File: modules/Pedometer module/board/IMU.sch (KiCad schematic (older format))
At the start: 2 parts, among them U3 LSM6DS3

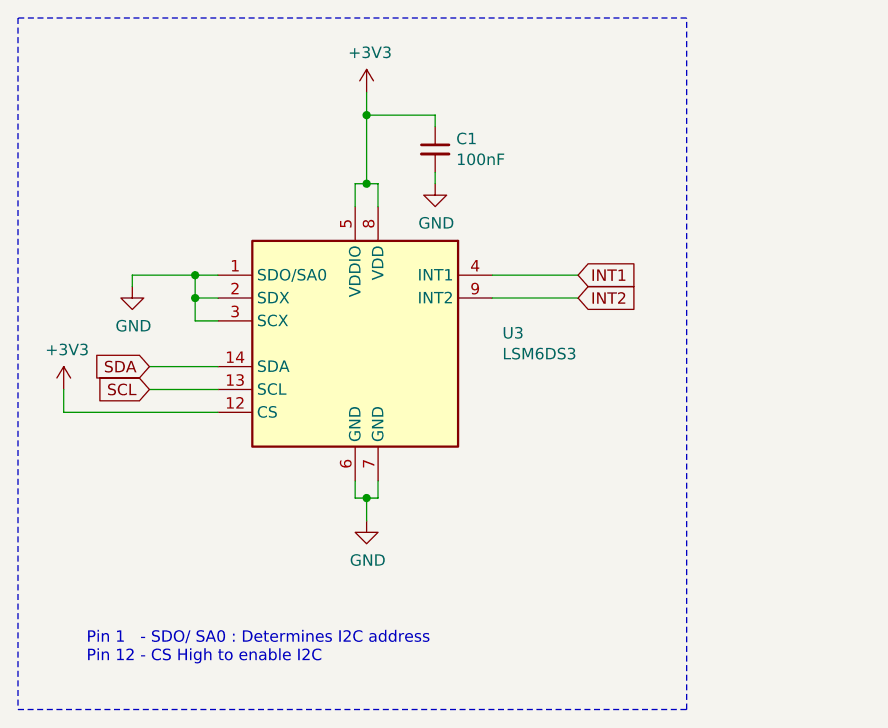
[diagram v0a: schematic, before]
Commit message: Fix I2C pullup resistor
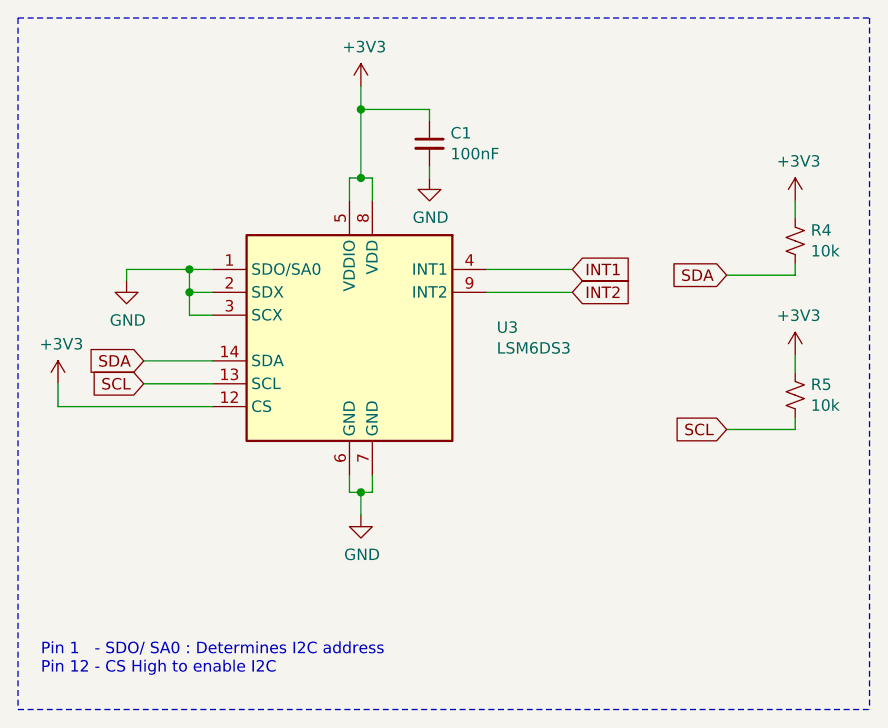
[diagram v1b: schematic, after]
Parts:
- added R4, R5: 10k, Resistor_SMD:R_0805_2012Metric_Pad1.20x1.40mm_HandSolder, symbol Device:R_Small_US
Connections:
- net +3V3: now also R4.1, R5.1
- net SCL: now also R5.2
- net SDA: now also R4.2
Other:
- moved on the sheet: C1, U3
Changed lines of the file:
@@
 Comment4 ""
 $EndDescr
+Wire Wire Line
+	5500 2750 5500 2850
+$Comp
+L power:GND #PWR09
+U 1 1 63A2C7F2
+P 5450 4225
+F 0 "#PWR09" H 5450 3975 50  0001 C CNN
+F 1 "GND" H 5455 4052 50  0000 C CNN
+F 2 "" H 5450 4225 50  0001 C CNN
+F 3 "" H 5450 4225 50  0001 C CNN
+	1    5450 4225
+	1    0    0    -1
+$EndComp
+Wire Wire Line
+	5400 4125 5400 4050
+Wire Wire Line
+	5400 4125 5450 4125
+Wire Wire Line
+	5450 4125 5450 4225
+Wire Wire Line
+	5500 4050 5500 4125
+Wire Wire Line
+	5500 4125 5450 4125
+Connection ~ 5450 4125
+Wire Wire Line
+	6000 3150 6375 3150
+Wire Wire Line
+	6000 3250 6375 3250
+Wire Wire Line
+	4800 3550 4500 3550
+Wire Wire Line
+	4800 3650 4500 3650
+Text GLabel 6375 3150 2    50   Input ~ 0
+INT1
+Text GLabel 6375 3250 2    50   Input ~ 0
+INT2
+Text GLabel 4500 3650 0    50   Input ~ 0
+SCL
+Text GLabel 4500 3550 0    50   Input ~ 0
+SDA
+$Comp
+L power:GND #PWR05
+U 1 1 63A35DA4
+P 4425 3200
+F 0 "#PWR05" H 4425 2950 50  0001 C CNN
+F 1 "GND" H 4430 3027 50  0000 C CNN
+F 2 "" H 4425 3200 50  0001 C CNN
+F 3 "" H 4425 3200 50  0001 C CNN
+	1    4425 3200
+	1    0    0    -1
+$EndComp
+Wire Wire Line
+	4425 3200 4425 3150
+Wire Wire Line
+	4800 3250 4700 3250
+Wire Wire Line
+	4700 3250 4700 3150
+Wire Wire Line
+	4700 3150 4800 3150
+Wire Wire Line
+	4800 3350 4700 3350
+Wire Wire Line
+	4700 3350 4700 3250
+Connection ~ 4700 3250
+Wire Wire Line
+	4425 3150 4700 3150
+Connection ~ 4700 3150
+Wire Wire Line
+	5400 2750 5400 2850
+$Comp
+L power:+3V3 #PWR07
+U 1 1 63A2BC7C
+P 5450 2350
+F 0 "#PWR07" H 5450 2200 50  0001 C CNN
+F 1 "+3V3" H 5465 2523 50  0000 C CNN
+F 2 "" H 5450 2350 50  0001 C CNN
+F 3 "" H 5450 2350 50  0001 C CNN
+	1    5450 2350
+	1    0    0    -1
+$EndComp
+$Comp
+L Device:C_Small C1
+U 1 1 63A39BBA
+P 5750 2600
+F 0 "C1" H 5842 2646 50  0000 L CNN
+F 1 "100nF" H 5842 2555 50  0000 L CNN
+F 2 "Capacitor_SMD:C_0805_2012Metric_Pad1.18x1.45mm_HandSolder" H 5750 2600 50  0001 C CNN
+F 3 "~" H 5750 2600 50  0001 C CNN
+	1    5750 2600
+	1    0    0    -1
+$EndComp
+Wire Wire Line
+	5400 2750 5450 2750
+$Comp
+L power:GND #PWR010
+U 1 1 63A3AF6F
+P 5750 2750
+F 0 "#PWR010" H 5750 2500 50  0001 C CNN
+F 1 "GND" H 5755 2577 50  0000 C CNN
+F 2 "" H 5750 2750 50  0001 C CNN
+F 3 "" H 5750 2750 50  0001 C CNN
+	1    5750 2750
+	1    0    0    -1
+$EndComp
+Wire Wire Line
+	5750 2750 5750 2700
+Connection ~ 5450 2750
+Wire Wire Line
+	5450 2750 5500 2750
+Wire Wire Line
+	5450 2350 5450 2450
+Wire Wire Line
+	5750 2500 5750 2450
+Wire Wire Line
+	5750 2450 5450 2450
+Connection ~ 5450 2450
+Wire Wire Line
+	5450 2450 5450 2750
+$Comp
+L power:+3V3 #PWR0109
+U 1 1 63A4A814
+P 4125 3650
+F 0 "#PWR0109" H 4125 3500 50  0001 C CNN
+F 1 "+3V3" H 4140 3823 50  0000 C CNN
+F 2 "" H 4125 3650 50  0001 C CNN
+F 3 "" H 4125 3650 50  0001 C CNN
+	1    4125 3650
+	1    0    0    -1
+$EndComp
+Wire Wire Line
+	4125 3650 4125 3750
+Wire Wire Line
+	4125 3750 4800 3750
+Text Notes 4050 4925 0    50   ~ 0
+Pin 1   - SDO/ SA0 : Determines I2C address\nPin 12 - CS High to enable I2C
+Wire Notes Line
+	3950 2050 3950 5075
+Wire Wire Line
+	7350 3800 7350 3850
+Wire Wire Line
+	7350 3525 7350 3600
+$Comp
+L power:+3V3 #PWR0110
+U 1 1 63B0AA74
+P 7350 3525
+F 0 "#PWR0110" H 7350 3375 50  0001 C CNN
+F 1 "+3V3" H 7365 3698 50  0000 C CNN
+F 2 "" H 7350 3525 50  0001 C CNN
+F 3 "" H 7350 3525 50  0001 C CNN
+	1    7350 3525
+	1    0    0    -1
+$EndComp
+Wire Wire Line
+	7350 3850 7050 3850
+Wire Wire Line
+	7350 3125 7350 3175
+Wire Wire Line
+	7350 2850 7350 2925
+$Comp
+L power:+3V3 #PWR0111
+U 1 1 63B08952
+P 7350 2850
+F 0 "#PWR0111" H 7350 2700 50  0001 C CNN
+F 1 "+3V3" H 7365 3023 50  0000 C CNN
+F 2 "" H 7350 2850 50  0001 C CNN
+F 3 "" H 7350 2850 50  0001 C CNN
+	1    7350 2850
+	1    0    0    -1
+$EndComp
+$Comp
+L Device:R_Small_US R4
+U 1 1 63B080DE
+P 7350 3025
+F 0 "R4" H 7418 3071 50  0000 L CNN
+F 1 "10k" H 7418 2980 50  0000 L CNN
+F 2 "Resistor_SMD:R_0805_2012Metric_Pad1.20x1.40mm_HandSolder" H 7350 3025 50  0001 C CNN
+F 3 "~" H 7350 3025 50  0001 C CNN
+	1    7350 3025
+	1    0    0    -1
+$EndComp
+Text GLabel 7050 3175 0    50   Input ~ 0
+SDA
+Text GLabel 7050 3850 0    50   Input ~ 0
+SCL
+Wire Wire Line
+	7350 3175 7050 3175
 $Comp
 L Sensor_Motion:LSM6DS3 U3
 U 1 1 63A2B005
-P 5425 3475
-F 0 "U3" H 6069 3521 50  0000 L CNN
-F 1 "LSM6DS3" H 6069 3430 50  0000 L CNN
-F 2 "Package_LGA:LGA-14_3x2.5mm_P0.5mm_LayoutBorder3x4y" H 5025 2775 50  0001 L CNN
-F 3 "www.st.com/resource/en/datasheet/lsm6ds3.pdf" H 5525 2825 50  0001 C CNN
-	1    5425 3475
-	1    0    0    -1
-$EndComp
-Wire Wire Line
-	5525 2775 5525 2875
-$Comp
-L power:GND #PWR09
-U 1 1 63A2C7F2
-P 5475 4250
-F 0 "#PWR09" H 5475 4000 50  0001 C CNN
-F 1 "GND" H 5480 4077 50  0000 C CNN
-F 2 "" H 5475 4250 50  0001 C CNN
-F 3 "" H 5475 4250 50  0001 C CNN
-	1    5475 4250
-	1    0    0    -1
-$EndComp
-Wire Wire Line
-	5425 4150 5425 4075
-Wire Wire Line
-	5425 4150 5475 4150
-Wire Wire Line
-	5475 4150 5475 4250
-Wire Wire Line
-	5525 4075 5525 4150
-Wire Wire Line
-	5525 4150 5475 4150
-Connection ~ 5475 4150
-Wire Wire Line
-	6025 3175 6400 3175
-Wire Wire Line
-	6025 3275 6400 3275
-Wire Wire Line
-	4825 3575 4525 3575
-Wire Wire Line
-	4825 3675 4525 3675
-Text GLabel 6400 3175 2    50   Input ~ 0
-INT1
-Text GLabel 6400 3275 2    50   Input ~ 0
-INT2
-Text GLabel 4525 3675 0    50   Input ~ 0
-SCL
-Text GLabel 4525 3575 0    50   Input ~ 0
-SDA
-$Comp
-L power:GND #PWR05
-U 1 1 63A35DA4
-P 4450 3225
-F 0 "#PWR05" H 4450 2975 50  0001 C CNN
-F 1 "GND" H 4455 3052 50  0000 C CNN
-F 2 "" H 4450 3225 50  0001 C CNN
-F 3 "" H 4450 3225 50  0001 C CNN
-	1    4450 3225
-	1    0    0    -1
-$EndComp
-Wire Wire Line
-	4450 3225 4450 3175
-Wire Wire Line
-	4825 3275 4725 3275
-Wire Wire Line
-	4725 3275 4725 3175
-Wire Wire Line
-	4725 3175 4825 3175
-Wire Wire Line
-	4825 3375 4725 3375
-Wire Wire Line
-	4725 3375 4725 3275
-Connection ~ 4725 3275
-Wire Wire Line
-	4450 3175 4725 3175
-Connection ~ 4725 3175
-Wire Wire Line
-	5425 2775 5425 2875
-$Comp
-L power:+3V3 #PWR07
-U 1 1 63A2BC7C
-P 5475 2375
-F 0 "#PWR07" H 5475 2225 50  0001 C CNN
-F 1 "+3V3" H 5490 2548 50  0000 C CNN
-F 2 "" H 5475 2375 50  0001 C CNN
-F 3 "" H 5475 2375 50  0001 C CNN
-	1    5475 2375
-	1    0    0    -1
-$EndComp
-$Comp
-L Device:C_Small C1
-U 1 1 63A39BBA
-P 5775 2625
-F 0 "C1" H 5867 2671 50  0000 L CNN
-F 1 "100nF" H 5867 2580 50  0000 L CNN
-F 2 "Capacitor_SMD:C_0805_2012Metric_Pad1.18x1.45mm_HandSolder" H 5775 2625 50  0001 C CNN
-F 3 "~" H 5775 2625 50  0001 C CNN
-	1    5775 2625
-	1    0    0    -1
-$EndComp
-Wire Wire Line
-	5425 2775 5475 2775
-$Comp
-L power:GND #PWR010
-U 1 1 63A3AF6F
-P 5775 2775
-F 0 "#PWR010" H 5775 2525 50  0001 C CNN
-F 1 "GND" H 5780 2602 50  0000 C CNN
-F 2 "" H 5775 2775 50  0001 C CNN
-F 3 "" H 5775 2775 50  0001 C CNN
-	1    5775 2775
-	1    0    0    -1
-$EndComp
-Wire Wire Line
-	5775 2775 5775 2725
-Connection ~ 5475 2775
-Wire Wire Line
-	5475 2775 5525 2775
-Wire Wire Line
-	5475 2375 5475 2475
-Wire Wire Line
-	5775 2525 5775 2475
-Wire Wire Line
-	5775 2475 5475 2475
-Connection ~ 5475 2475
-Wire Wire Line
-	5475 2475 5475 2775
-$Comp
-L power:+3V3 #PWR0109
-U 1 1 63A4A814
-P 4150 3675
-F 0 "#PWR0109" H 4150 3525 50  0001 C CNN
-F 1 "+3V3" H 4165 3848 50  0000 C CNN
-F 2 "" H 4150 3675 50  0001 C CNN
-F 3 "" H 4150 3675 50  0001 C CNN
-	1    4150 3675
-	1    0    0    -1
-$EndComp
-Wire Wire Line
-	4150 3675 4150 3775
-Wire Wire Line
-	4150 3775 4825 3775
-Text Notes 4250 4875 0    50   ~ 0
-Pin 1   - SDO/ SA0 : Determines I2C address\nPin 12 - CS High to enable I2C
-Wire Notes Line
-	3950 5075 6875 5075
-Wire Notes Line
-	6875 5075 6875 2050
-Wire Notes Line
-	6875 2050 3950 2050
-Wire Notes Line
-	3950 2050 3950 5075
+P 5400 3450
+F 0 "U3" H 6044 3496 50  0000 L CNN
+F 1 "LSM6DS3" H 6044 3405 50  0000 L CNN
+F 2 "Package_LGA:LGA-14_3x2.5mm_P0.5mm_LayoutBorder3x4y" H 5000 2750 50  0001 L CNN
+F 3 "www.st.com/resource/en/datasheet/lsm6ds3.pdf" H 5500 2800 50  0001 C CNN
+	1    5400 3450
+	1    0    0    -1
+$EndComp
+Wire Notes Line
+	7675 2050 7675 5075
+Wire Notes Line
+	3950 2050 7675 2050
+Wire Notes Line
+	3950 5075 7675 5075
+$Comp
+L Device:R_Small_US R5
+U 1 1 63B123DC
+P 7350 3700
+F 0 "R5" H 7418 3746 50  0000 L CNN
+F 1 "10k" H 7418 3655 50  0000 L CNN
+F 2 "Resistor_SMD:R_0805_2012Metric_Pad1.20x1.40mm_HandSolder" H 7350 3700 50  0001 C CNN
+F 3 "~" H 7350 3700 50  0001 C CNN
+	1    7350 3700
+	1    0    0    -1
+$EndComp
 $EndSCHEMATC
